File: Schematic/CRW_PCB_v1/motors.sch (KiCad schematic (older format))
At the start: 20 parts

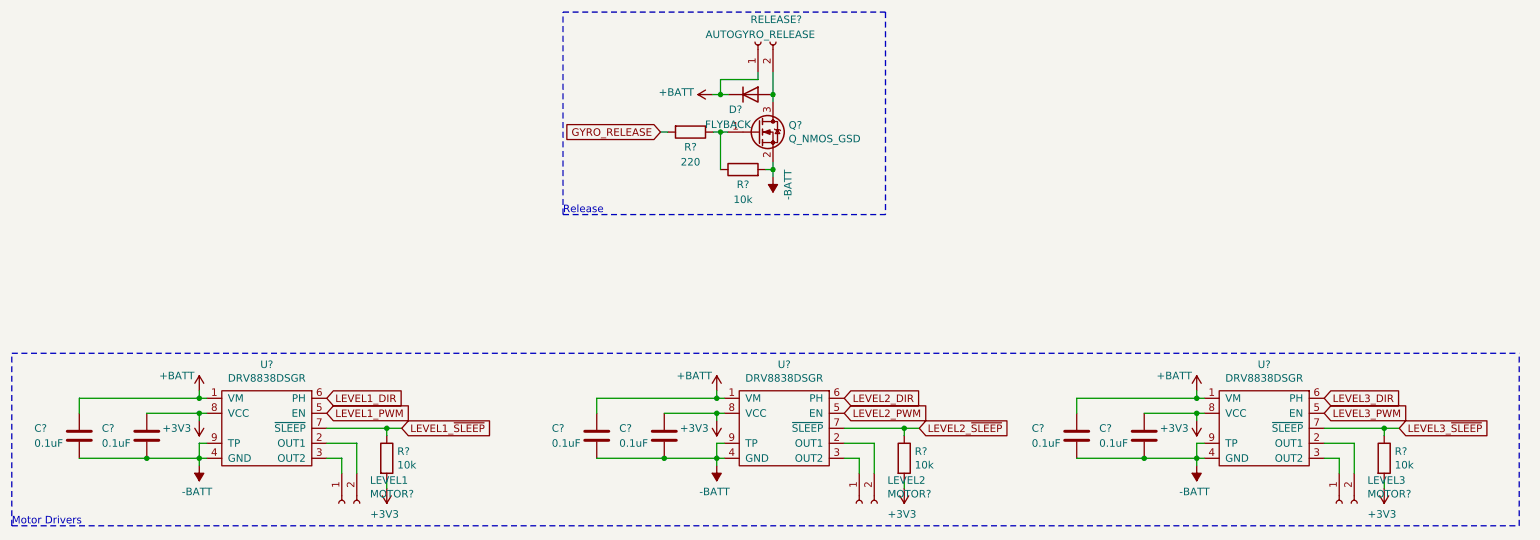
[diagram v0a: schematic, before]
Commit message: Added Hotwire Connection
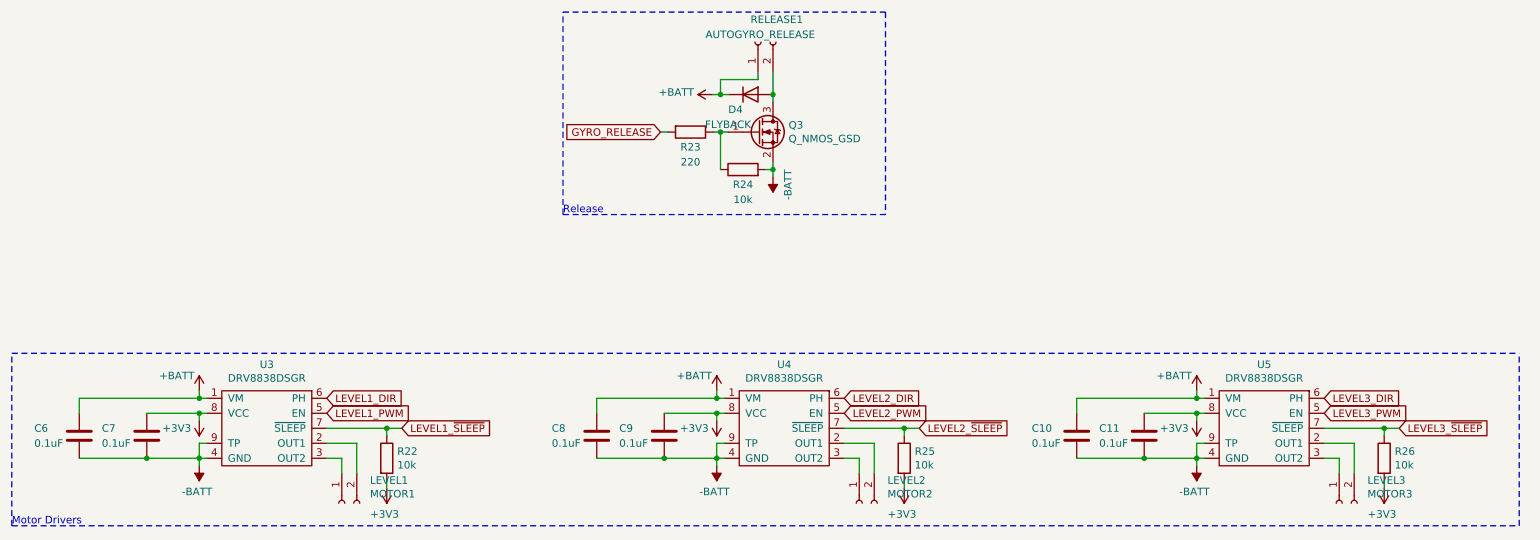
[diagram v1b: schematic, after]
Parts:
- gave numbers to parts that had none: 20
